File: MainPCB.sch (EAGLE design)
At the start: 38 parts, among them J2 DCJ0202

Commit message: yayyy pinsssss
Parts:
- added C12, C13: 10pF, SparkFun-Capacitors:10UF-0805-10V-10%
- added D1: GREEN-0603, Seeed-LED:SMD-LED-CLEAR-GREEN(0603)
- added D2: BLUE-0603, Seeed-LED:SMD-LED-CLEAR-BLUE(0603)
- added H5, H6, H7, H8: STAND-OFF, SparkFun-Hardware:STAND-OFF
- added R10, R11: 100, SparkFun-Resistors:100OHM-0603-1/4W-5%
- added X1: 8MHz, IQD-Frequency-Products:CRYSTALS-NOGND-HC49
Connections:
- new net BUTT_DOWN: U$1.PB14
- new net BUTT_SEL: U$1.PB12
- new net BUTT_UP: U$1.PB13
- new net COLOUT_1: U$1.PC10
- new net COLOUT_2: U$1.PC11
- new net COLOUT_3: U$1.PC12
- new net COLOUT_4: U$1.PB11
- new net COLOUT_5: U$1.PB5
- new net COLOUT_6: U$1.PB6
- new net COLOUT_7: U$1.PB7
- new net COLOUT_8: U$1.PB8
- new net COLOUT_9: U$1.PB9
- new net N$1: C12.2, U$1.PH0-OSC_IN, X1.1
- new net N$2: C13.1, U$1.PH1-OSC_OUT, X1.2
- new net N$4: R10.1, U$1.PA12
- new net N$5: D1.+, R10.2
- new net N$6: R11.1, U$1.PA11
- new net N$7: D2.+, R11.2
- net GND: now also C12.1, C13.2, D1.-, D2.-
- net MOSI: now also U$1.PC3; no longer U$1.PB15
- net RX_ESP: now also U$1.PA10; no longer U$1.PB6
- net SCLK: now also U$1.PB10; no longer U$1.PB13
- net TX_ESP: now also U$1.PA9; no longer U$1.PB7

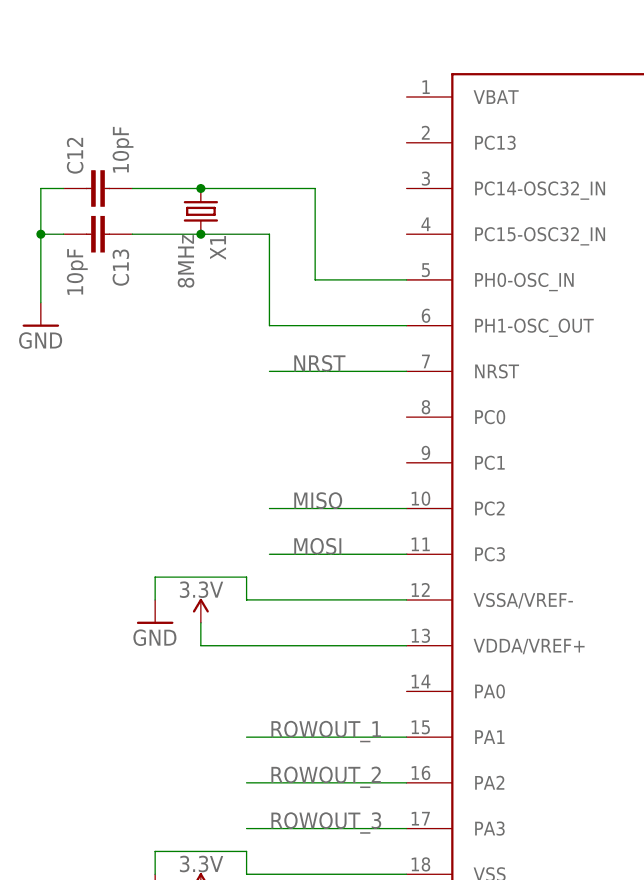
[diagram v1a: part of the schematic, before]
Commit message: added reset switch
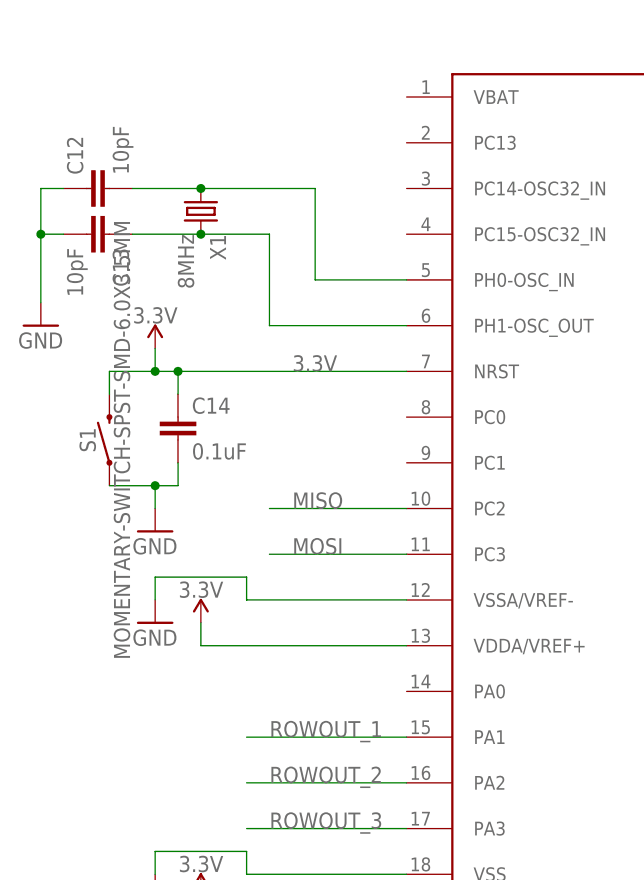
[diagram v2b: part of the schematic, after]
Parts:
- added C14: 0.1uF, SparkFun-Capacitors:0.1UF-0603-25V-(+80/-20%)
- added S1: MOMENTARY-SWITCH-SPST-SMD-6.0X3.5MM, SparkFun-Switches:MOMENTARY-SWITCH-SPST-SMD-6.0X3.5MM
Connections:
- net 3.3V: now also C14.1, S1.2, U$1.NRST
- net GND: now also C14.2, S1.1
- net NRST: no longer U$1.NRST
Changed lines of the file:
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@@
 <part name="R11" library="SparkFun-Resistors" library_urn="urn:adsk.eagle:library:532" deviceset="100OHM" device="-0603-1/4W-5%" package3d_urn="urn:adsk.eagle:package:39650/1" value="100"/>
 <part name="GND28" library="supply1" library_urn="urn:adsk.eagle:library:371" deviceset="GND" device=""/>
+<part name="C14" library="SparkFun-Capacitors" library_urn="urn:adsk.eagle:library:510" deviceset="0.1UF" device="-0603-25V-(+80/-20%)" package3d_urn="urn:adsk.eagle:package:37414/1" value="0.1uF"/>
+<part name="S1" library="SparkFun-Switches" library_urn="urn:adsk.eagle:library:535" deviceset="MOMENTARY-SWITCH-SPST" device="-SMD-6.0X3.5MM" package3d_urn="urn:adsk.eagle:package:40165/1"/>
+<part name="SUPPLY12" library="SparkFun-PowerSymbols" library_urn="urn:adsk.eagle:library:530" deviceset="3.3V" device=""/>
+<part name="GND29" library="supply1" library_urn="urn:adsk.eagle:library:371" deviceset="GND" device=""/>
 </parts>
 <sheets>
@@
 <instance part="GND28" gate="1" x="182.88" y="53.34">
 <attribute name="VALUE" x="180.34" y="50.8" size="1.778" layer="96"/>
+</instance>
+<instance part="C14" gate="G$1" x="25.4" y="132.08">
+<attribute name="NAME" x="26.924" y="135.001" size="1.778" layer="95" font="vector"/>
+<attribute name="VALUE" x="26.924" y="129.921" size="1.778" layer="96" font="vector"/>
+</instance>
+<instance part="S1" gate="G$1" x="17.78" y="132.08" rot="R90">
+<attribute name="NAME" x="16.256" y="132.08" size="1.778" layer="95" font="vector" rot="R90" align="bottom-center"/>
+</instance>
+<instance part="SUPPLY12" gate="G$1" x="22.86" y="142.24">
+<attribute name="VALUE" x="22.86" y="145.034" size="1.778" layer="96" align="bottom-center"/>
+</instance>
+<instance part="GND29" gate="1" x="22.86" y="121.92">
+<attribute name="VALUE" x="20.32" y="119.38" size="1.778" layer="96"/>
 </instance>
 </instances>
@@
 <junction x="182.88" y="60.96"/>
 </segment>
+<segment>
+<pinref part="S1" gate="G$1" pin="1"/>
+<pinref part="GND29" gate="1" pin="GND"/>
+<wire x1="17.78" y1="127" x2="22.86" y2="127" width="0.1524" layer="91"/>
+<wire x1="22.86" y1="127" x2="22.86" y2="124.46" width="0.1524" layer="91"/>
+<pinref part="C14" gate="G$1" pin="2"/>
+<wire x1="22.86" y1="127" x2="25.4" y2="127" width="0.1524" layer="91"/>
+<wire x1="25.4" y1="127" x2="25.4" y2="129.54" width="0.1524" layer="91"/>
+<junction x="22.86" y="127"/>
+</segment>
 </net>
 <net name="+5V" class="0">
@@
 <pinref part="SUPPLY11" gate="G$1" pin="3.3V"/>
 </segment>
+<segment>
+<pinref part="U$1" gate="G$1" pin="NRST"/>
+<wire x1="50.8" y1="139.7" x2="25.4" y2="139.7" width="0.1524" layer="91"/>
+<label x="38.1" y="139.7" size="1.778" layer="95"/>
+<pinref part="SUPPLY12" gate="G$1" pin="3.3V"/>
+<wire x1="25.4" y1="139.7" x2="22.86" y2="139.7" width="0.1524" layer="91"/>
+<wire x1="22.86" y1="139.7" x2="22.86" y2="142.24" width="0.1524" layer="91"/>
+<pinref part="C14" gate="G$1" pin="1"/>
+<wire x1="25.4" y1="137.16" x2="25.4" y2="139.7" width="0.1524" layer="91"/>
+<junction x="25.4" y="139.7"/>
+<pinref part="S1" gate="G$1" pin="2"/>
+<wire x1="17.78" y1="137.16" x2="17.78" y2="139.7" width="0.1524" layer="91"/>
+<wire x1="17.78" y1="139.7" x2="22.86" y2="139.7" width="0.1524" layer="91"/>
+<junction x="22.86" y="139.7"/>
+</segment>
 </net>
 <net name="N$3" class="0">
@@
 <net name="NRST" class="0">
 <segment>
-<pinref part="U$1" gate="G$1" pin="NRST"/>
-<wire x1="50.8" y1="139.7" x2="35.56" y2="139.7" width="0.1524" layer="91"/>
-<label x="38.1" y="139.7" size="1.778" layer="95"/>
-</segment>
-<segment>
 <pinref part="JP2" gate="A" pin="5"/>

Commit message: added some pins for buttons
also changed the layout slightly
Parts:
- removed JP5: (no value), pinhead:PINHD-1X18
- added H9: STAND-OFF, SparkFun-Hardware:STAND-OFF
- added J3: FEMALE 2x3, SparkFun-Connectors:CONN_03X2FEMALE
- added U$11, U$12, U$8: TMUX1112PWR, SeniorDesignParts:TMUX1112PWR
- added U$13, U$14, U$15, U$16, U$17, U$18: 3PINCONN, SeniorDesignParts:3PINCONN
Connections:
- new net COL1: U$14.A
- new net COL2: U$14.B
- new net COL3: U$14.C
- new net COL4: U$16.A
- new net COL5: U$16.B
- new net COL6: U$16.C
- new net COL7: U$18.A
- new net COL8: U$18.B
- new net COL9: U$18.C
- net BUTT_DOWN: now also J3.5
- net BUTT_SEL: now also J3.1
- net BUTT_UP: now also J3.3
- net GND: now also J3.2, J3.4, J3.6
- net ROW1: now also U$13.A; no longer JP5.1
- net ROW2: now also U$13.B; no longer JP5.2
- net ROW3: now also U$13.C; no longer JP5.3
- net ROW4: now also U$15.A; no longer JP5.4
- net ROW5: now also U$15.B; no longer JP5.5
- net ROW6: now also U$15.C; no longer JP5.6
- net ROW7: now also U$17.A; no longer JP5.7
- net ROW8: now also U$17.B; no longer JP5.8
- net ROW9: now also U$17.C; no longer JP5.9

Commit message: the finer things
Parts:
- added R12, R13: 100k, SparkFun-Resistors:100KOHM-0603-1/10W-1%
- added R14, R15, R16: 3.3k, SparkFun-Resistors:3.3KOHM-0603-1/10W-1%
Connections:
- new net N$9: R13.2, U$1.BOOT0
- net 3.3V: now also R12.2, R14.2, R15.2, R16.2, U$1.VBAT; no longer C14.1, S1.2, U$1.NRST
- net BUTT_DOWN: now also R14.1
- net BUTT_SEL: now also R16.1
- net BUTT_UP: now also R15.1
- net GND: now also R13.1, U$11.GND, U$12.GND, U$8.GND
- net NRST: now also C14.1, R12.1, S1.2, U$1.NRST
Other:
- moved on the sheet: C12, C13, C14, S1, X1

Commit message: schematic DONE
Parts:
- added C15, C16, C17, C18, C19, C20, C21, C22, C23: 10nF, SparkFun-Capacitors:10NF-0603-50V-10%
- R1, R2, R3, R4, R5, R6, R7, R8, R9: value 1k -> 1M
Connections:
- net +5V: no longer U$10.VCC+, U$2.VCC+, U$9.VCC+
- net 3.3V: now also U$10.VCC+, U$11.VDD, U$12.VDD, U$2.VCC+, U$8.VDD, U$9.VCC+
- net COL1: now also U$8.S1
- net COL2: now also U$8.S2
- net COL3: now also U$8.S3
- net COL4: now also U$11.S1
- net COL5: now also U$11.S2
- net COL6: now also U$11.S3
- net COL7: now also U$12.S1
- net COL8: now also U$12.S2
- net COL9: now also U$12.S3
- net COLOUT_1: now also U$8.SEL1
- net COLOUT_2: now also U$8.SEL2
- net COLOUT_3: now also U$8.SEL3
- net COLOUT_4: now also U$11.SEL1
- net COLOUT_5: now also U$11.SEL2
- net COLOUT_6: now also U$11.SEL3
- net COLOUT_7: now also U$12.SEL1
- net COLOUT_8: now also U$12.SEL2
- net COLOUT_9: now also U$12.SEL3
- net GND: now also U$11.D1, U$11.D2, U$11.D3, U$12.D1, U$12.D2, U$12.D3, U$8.D1, U$8.D2, U$8.D3
- net ROW1: now also C23.2
- net ROW2: now also C22.2
- net ROW3: now also C21.2
- net ROW4: now also C17.2
- net ROW5: now also C16.2
- net ROW6: now also C15.2
- net ROW7: now also C20.2
- net ROW8: now also C19.2
- net ROW9: now also C18.2
- net ROWOUT_1: now also C23.1
- net ROWOUT_2: now also C22.1
- net ROWOUT_3: now also C21.1
- net ROWOUT_4: now also C17.1
- net ROWOUT_5: now also C16.1
- net ROWOUT_6: now also C15.1
- net ROWOUT_7: now also C20.1
- net ROWOUT_8: now also C19.1
- net ROWOUT_9: now also C18.1
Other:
- moved on the sheet: R1, R2, R3, R4, R5, R6, R7, R8, R9, U$10

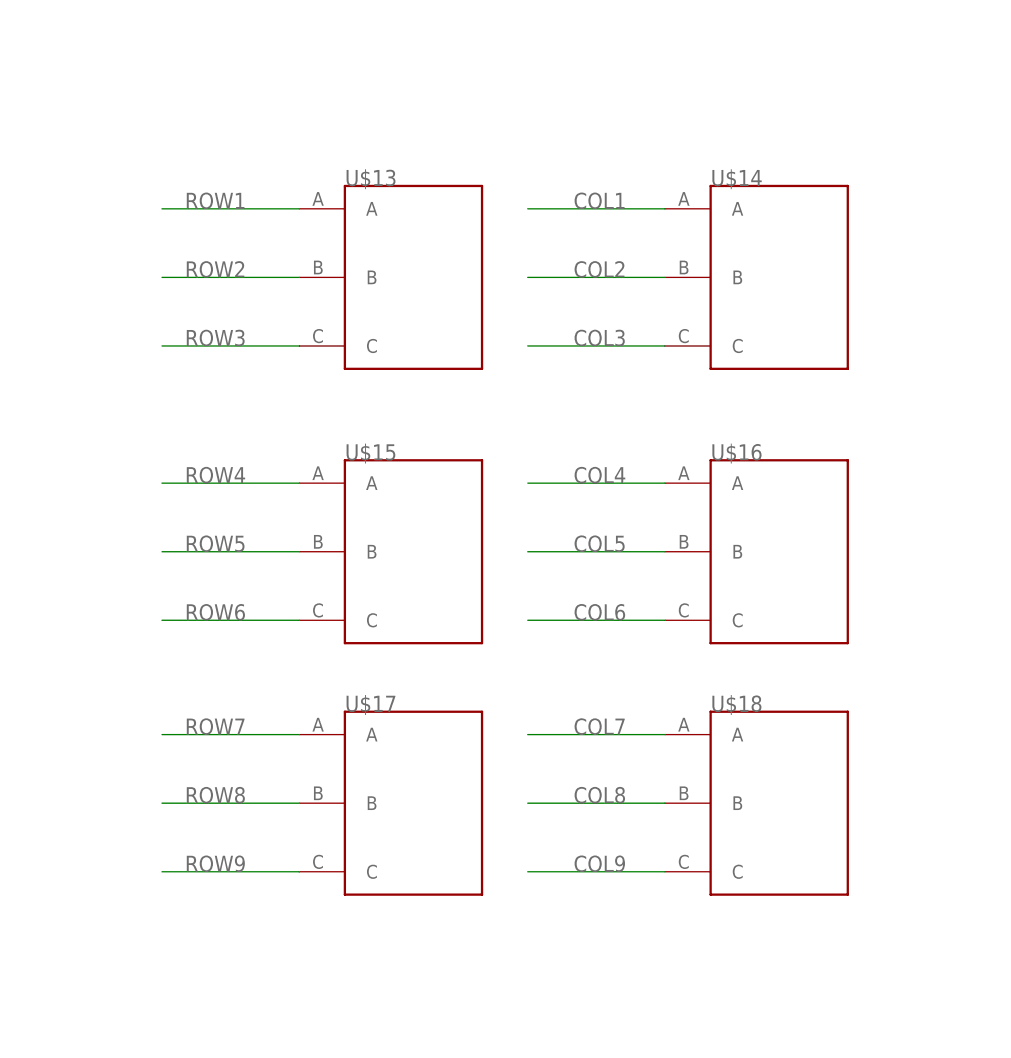
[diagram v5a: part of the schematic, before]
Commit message: changed layout
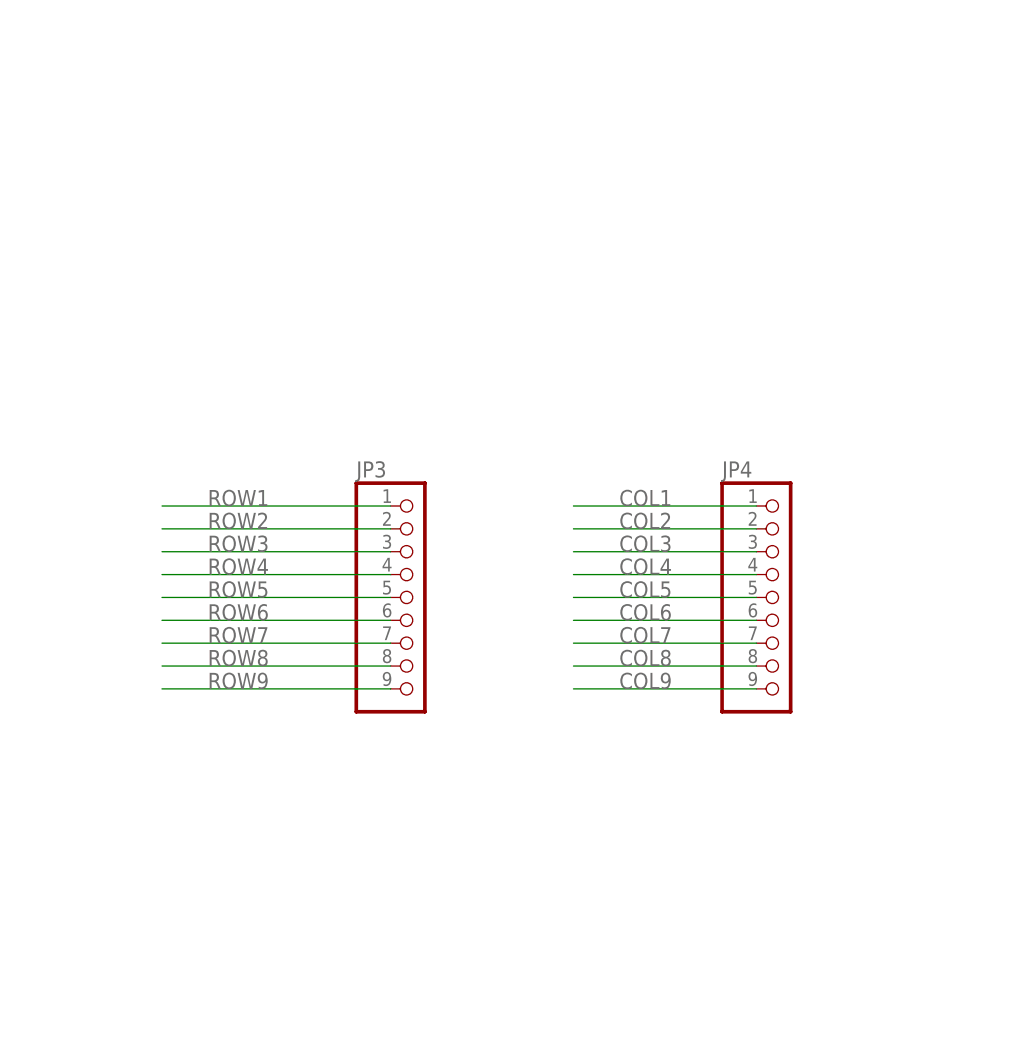
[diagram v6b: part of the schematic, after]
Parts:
- removed U$13, U$14, U$15, U$16, U$17, U$18: 3PINCONN, SeniorDesignParts:3PINCONN
- added JP3, JP4: (no value), pinhead:PINHD-1X9
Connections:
- net COL1: now also JP4.1; no longer U$14.A
- net COL2: now also JP4.2; no longer U$14.B
- net COL3: now also JP4.3; no longer U$14.C
- net COL4: now also JP4.4; no longer U$16.A
- net COL5: now also JP4.5; no longer U$16.B
- net COL6: now also JP4.6; no longer U$16.C
- net COL7: now also JP4.7; no longer U$18.A
- net COL8: now also JP4.8; no longer U$18.B
- net COL9: now also JP4.9; no longer U$18.C
- net ROW1: now also JP3.1; no longer U$13.A
- net ROW2: now also JP3.2; no longer U$13.B
- net ROW3: now also JP3.3; no longer U$13.C
- net ROW4: now also JP3.4; no longer U$15.A
- net ROW5: now also JP3.5; no longer U$15.B
- net ROW6: now also JP3.6; no longer U$15.C
- net ROW7: now also JP3.7; no longer U$17.A
- net ROW8: now also JP3.8; no longer U$17.B
- net ROW9: now also JP3.9; no longer U$17.C

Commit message: savey save saved save
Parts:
- added C24, C25, C26: 0.1uF, SparkFun-Capacitors:0.1UF-0603-100V-10%
- added R17: 1k, SparkFun-Resistors:1KOHM-0603-1/10W-1%
- added R18, R19: 100, SparkFun-Resistors:100KOHM-0603-1/10W-1%
- added S2, S3: MOMENTARY-SWITCH-SPST-SMD-6.0X3.5MM, SparkFun-Switches:MOMENTARY-SWITCH-SPST-SMD-6.0X3.5MM
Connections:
- new net EN: C24.1, C26.1, R17.1, S2.2, U$7.EN
- new net IO0: C25.1, S3.2, U$7.IO0
- new net N$10: R19.2, U$7.RXD0
- new net N$8: R18.2, U$7.TXD0
- net 3.3V: now also R17.2
- net GND: now also C24.2, C25.2, C26.2, S2.1, S3.1
- net RX_ESP: now also R19.1; no longer U$7.RXD0
- net TX_ESP: now also R18.1; no longer U$7.TXD0
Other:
- note added: "5V->3V Conversion"
- note added: "9V input Barrel Jack"
- note added: "9V->5V Conversion"
- note added: "Antenna Board Connections"
- note added: "Button Connections"
- note added: "PhotoDiode Connectors"
- note added: "Switch for Columns"
- note added: "Transimpedence Amplifier for Rows"

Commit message: she done
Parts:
- added H10: STAND-OFF, SparkFun-Hardware:STAND-OFF
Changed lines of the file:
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@@
 <part name="R18" library="SparkFun-Resistors" library_urn="urn:adsk.eagle:library:532" deviceset="100KOHM" device="-0603-1/10W-1%" package3d_urn="urn:adsk.eagle:package:39650/1" value="100"/>
 <part name="R19" library="SparkFun-Resistors" library_urn="urn:adsk.eagle:library:532" deviceset="100KOHM" device="-0603-1/10W-1%" package3d_urn="urn:adsk.eagle:package:39650/1" value="100"/>
+<part name="H10" library="SparkFun-Hardware" library_urn="urn:adsk.eagle:library:519" deviceset="STAND-OFF" device="" package3d_urn="urn:adsk.eagle:package:38630/1"/>
 </parts>
 <sheets>
@@
 <attribute name="VALUE" x="492.76" y="128.524" size="1.778" layer="96" font="vector" rot="R180" align="top-center"/>
 </instance>
+<instance part="H10" gate="G$1" x="215.9" y="30.48"/>
 </instances>
 <busses>
